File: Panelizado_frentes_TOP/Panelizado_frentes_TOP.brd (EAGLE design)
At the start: 130 x 100 mm, 17 parts, among them J2 F0504-H-05-10G-R, Q4 BSS138, Q5 BSS138, Q6 BSS138

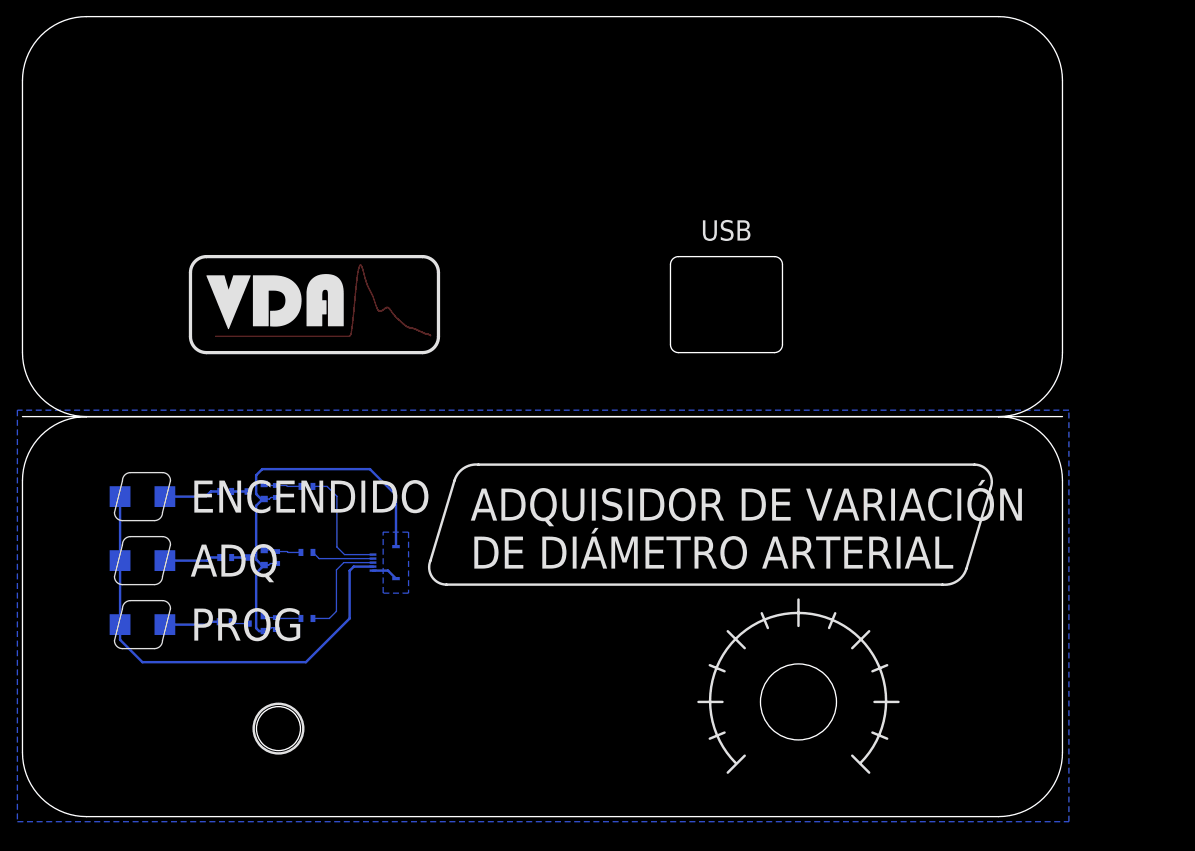
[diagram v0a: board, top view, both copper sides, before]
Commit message: BOM del adquisidor listo
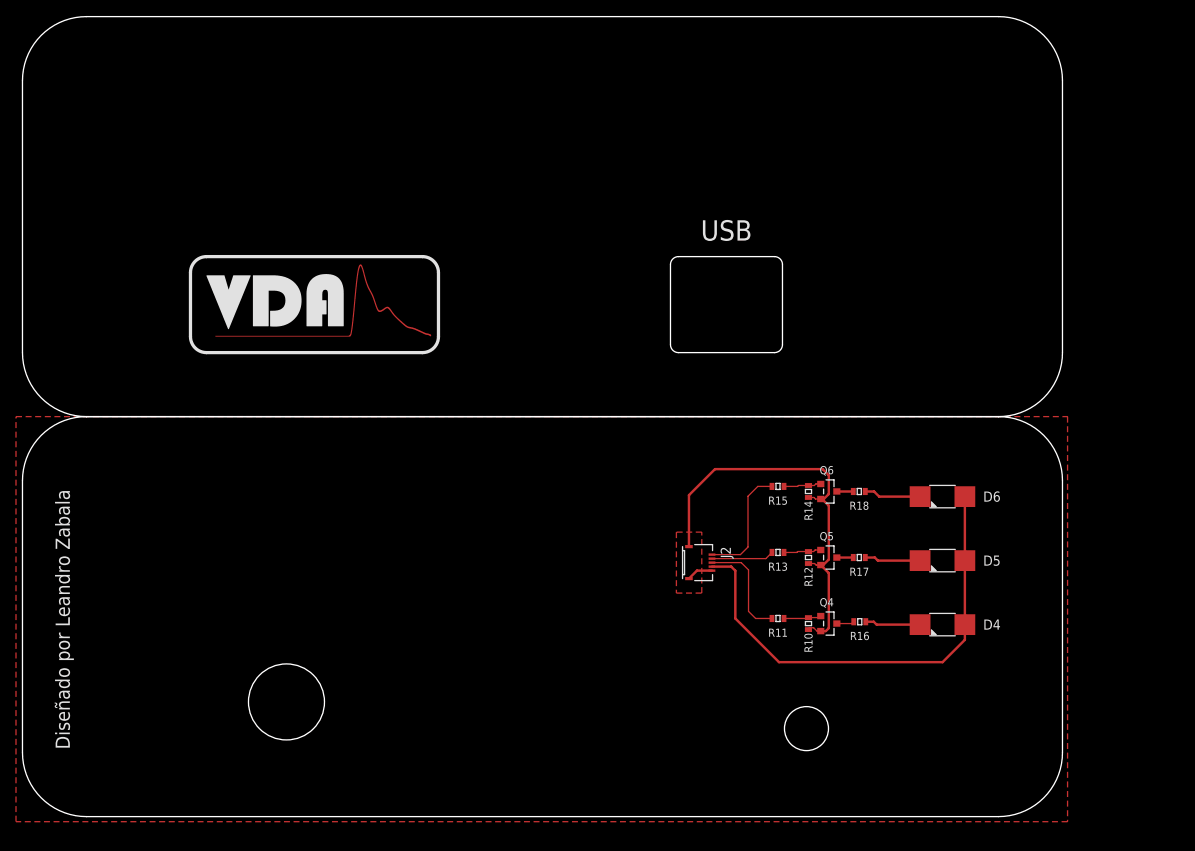
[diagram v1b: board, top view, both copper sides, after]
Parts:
- moved D4 100.0 mm to (115.0, 24.0), flipped to the top
- moved D5 100.0 mm to (115.0, 32.0), flipped to the top
- moved D6 100.0 mm to (115.0, 40.0), flipped to the top
- moved R16 79.3 mm to (104.7, 24.4), flipped to the top
- moved R17 79.2 mm to (104.6, 32.4), flipped to the top
- moved R18 79.2 mm to (104.6, 40.6), flipped to the top
- moved Q4 71.6 mm to (100.8, 24.1), flipped to the top
- moved Q5 71.6 mm to (100.8, 32.4), flipped to the top
- moved Q6 71.6 mm to (100.8, 40.6), flipped to the top
- moved R10 66.5 mm to (98.2, 24.1), flipped to the top
- moved R12 66.5 mm to (98.2, 32.4), flipped to the top
- moved R14 66.5 mm to (98.2, 40.6), flipped to the top
- moved R11 58.9 mm to (94.4, 24.8), flipped to the top
- moved R13 58.9 mm to (94.4, 33.0), flipped to the top
- moved R15 58.9 mm to (94.4, 41.3), flipped to the top
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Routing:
- added copper zone on layer 1, net GND
- removed copper zone on layer 16, net GND
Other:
- outline, holes or cut-outs redrawn
- board text removed: "V-SCORING"
